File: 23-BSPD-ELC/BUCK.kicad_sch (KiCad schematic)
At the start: 0 parts

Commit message: Revision changes and updates to some footprints
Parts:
- added C32, C33: 10uF, Capacitor_SMD:C_0603_1608Metric_Pad1.08x0.95mm_HandSolder, symbol Device:C
- added C34, C35: 100nF, Capacitor_SMD:C_0603_1608Metric_Pad1.08x0.95mm_HandSolder, symbol Device:C
- added C36, C37: 22uF, Capacitor_SMD:C_0603_1608Metric_Pad1.08x0.95mm_HandSolder, symbol Device:C
- added L2: 4u7, Inductor_SMD:L_Sunlord_MWSA0518_5.4x5.2mm, symbol Device:L
- added R56, R57: 10K, Resistor_SMD:R_0603_1608Metric_Pad0.98x0.95mm_HandSolder, symbol Device:R
- added R58: 54.9K, Resistor_SMD:R_0603_1608Metric_Pad0.98x0.95mm_HandSolder, symbol Device:R
- added U19: LMR51420, Package_TO_SOT_SMD:SOT-23-6, symbol Regulator_Switching:TPS562200
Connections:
- new net 5V_out: C36.1, C37.1, L2.2, R58.2
- new net EN: R56.2, U19.5 (EN)
- new net GND: C32.2, C33.2, C34.2, C36.2, C37.2, R57.2, U19.1 (GND)
- new net SW: C35.1, L2.1, U19.2 (SW)
- new net VBST: C35.2, U19.6 (VBST)
- new net VFB: R57.1, R58.1, U19.4 (VFB)
- new net V_in: C32.1, C33.1, C34.1, R56.1, U19.3 (VIN)
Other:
- note added: "Pull EN high to enable (19V tolerant)"

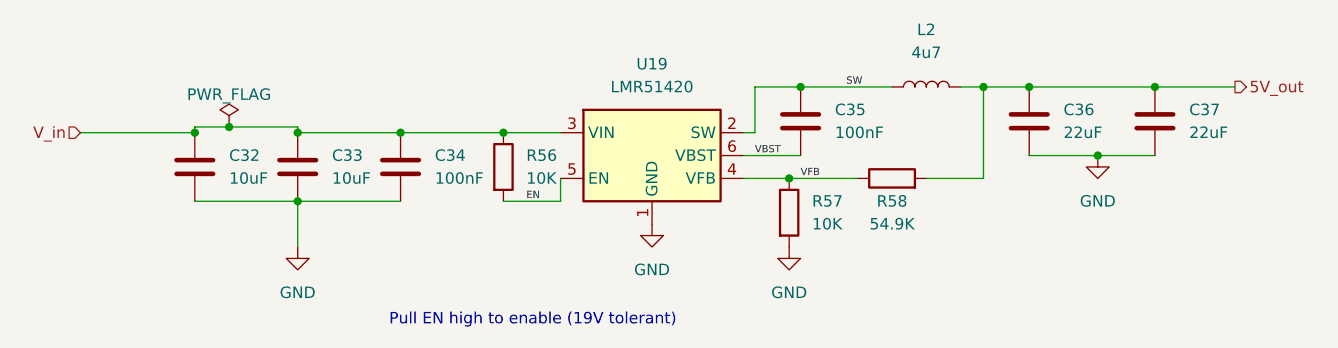
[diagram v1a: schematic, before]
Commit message: Updated pcb layout; Watchdog on board still in progress
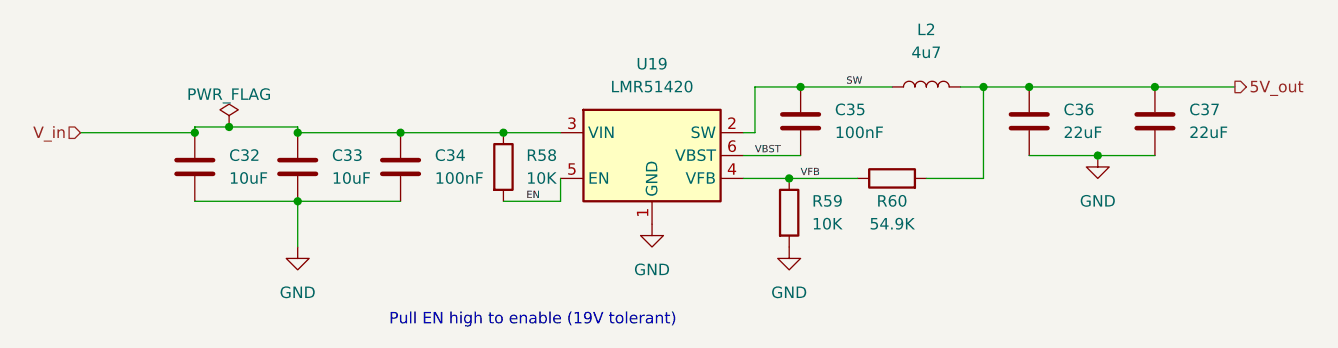
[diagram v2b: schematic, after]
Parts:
- renumbered R56 to R58, R57 to R59, R58 to R60
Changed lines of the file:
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@@
   (symbol (lib_id "Device:R") (at 170.18 84.455 90) (unit 1)
     (in_bom yes) (on_board yes)
-    (property "Reference" "R58" (id 0) (at 170.18 86.995 90))
+    (property "Reference" "R60" (id 0) (at 170.18 86.995 90))
     (property "Value" "54.9K" (id 1) (at 170.18 89.535 90))
     (property "Footprint" "Resistor_SMD:R_0603_1608Metric_Pad0.98x0.95mm_HandSolder" (id 2) (at 170.18 86.233 90)
@@
   (symbol (lib_id "Device:R") (at 127 83.185 0) (unit 1)
     (in_bom yes) (on_board yes) (fields_autoplaced)
-    (property "Reference" "R56" (id 0) (at 129.54 81.9149 0)
+    (property "Reference" "R58" (id 0) (at 129.54 81.9149 0)
       (effects (font (size 1.27 1.27)) (justify left))
     )
@@
   (symbol (lib_id "Device:R") (at 158.75 88.265 0) (unit 1)
     (in_bom yes) (on_board yes) (fields_autoplaced)
-    (property "Reference" "R57" (id 0) (at 161.29 86.9949 0)
+    (property "Reference" "R59" (id 0) (at 161.29 86.9949 0)
       (effects (font (size 1.27 1.27)) (justify left))
     )

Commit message: BSPD layout
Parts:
- renumbered C32 to C35, C33 to C36, C34 to C37, C35 to C38, C36 to C39, C37 to C40, R58 to R59, R59 to R60, R60 to R61, U19 to U20
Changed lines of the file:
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@@
   (symbol (lib_id "Device:C") (at 199.39 78.105 0) (unit 1)
     (in_bom yes) (on_board yes) (fields_autoplaced)
-    (property "Reference" "C37" (id 0) (at 203.2 76.8349 0)
+    (property "Reference" "C40" (id 0) (at 203.2 76.8349 0)
       (effects (font (size 1.27 1.27)) (justify left))
     )
@@
   (symbol (lib_id "power:GND") (at 193.04 81.915 0) (unit 1)
     (in_bom yes) (on_board yes) (fields_autoplaced)
-    (property "Reference" "#PWR0162" (id 0) (at 193.04 88.265 0)
+    (property "Reference" "#PWR0169" (id 0) (at 193.04 88.265 0)
       (effects (font (size 1.27 1.27)) hide)
     )
@@
   (symbol (lib_id "Device:C") (at 185.42 78.105 0) (unit 1)
     (in_bom yes) (on_board yes) (fields_autoplaced)
-    (property "Reference" "C36" (id 0) (at 189.23 76.8349 0)
+    (property "Reference" "C39" (id 0) (at 189.23 76.8349 0)
       (effects (font (size 1.27 1.27)) (justify left))
     )
@@
   (symbol (lib_id "Device:C") (at 92.71 83.185 0) (unit 1)
     (in_bom yes) (on_board yes) (fields_autoplaced)
-    (property "Reference" "C32" (id 0) (at 96.52 81.9149 0)
+    (property "Reference" "C35" (id 0) (at 96.52 81.9149 0)
       (effects (font (size 1.27 1.27)) (justify left))
     )
@@
   (symbol (lib_id "Device:C") (at 104.14 83.185 0) (unit 1)
     (in_bom yes) (on_board yes) (fields_autoplaced)
-    (property "Reference" "C33" (id 0) (at 107.95 81.9149 0)
+    (property "Reference" "C36" (id 0) (at 107.95 81.9149 0)
       (effects (font (size 1.27 1.27)) (justify left))
     )
@@
   (symbol (lib_id "Device:C") (at 115.57 83.185 0) (unit 1)
     (in_bom yes) (on_board yes) (fields_autoplaced)
-    (property "Reference" "C34" (id 0) (at 119.38 81.9149 0)
+    (property "Reference" "C37" (id 0) (at 119.38 81.9149 0)
       (effects (font (size 1.27 1.27)) (justify left))
     )
@@
   (symbol (lib_id "power:GND") (at 143.51 89.535 0) (unit 1)
     (in_bom yes) (on_board yes) (fields_autoplaced)
-    (property "Reference" "#PWR0160" (id 0) (at 143.51 95.885 0)
+    (property "Reference" "#PWR0167" (id 0) (at 143.51 95.885 0)
       (effects (font (size 1.27 1.27)) hide)
     )
@@
   (symbol (lib_id "Device:R") (at 170.18 84.455 90) (unit 1)
     (in_bom yes) (on_board yes)
-    (property "Reference" "R60" (id 0) (at 170.18 86.995 90))
+    (property "Reference" "R61" (id 0) (at 170.18 86.995 90))
     (property "Value" "54.9K" (id 1) (at 170.18 89.535 90))
     (property "Footprint" "Resistor_SMD:R_0603_1608Metric_Pad0.98x0.95mm_HandSolder" (id 2) (at 170.18 86.233 90)
@@
   (symbol (lib_id "Device:R") (at 127 83.185 0) (unit 1)
     (in_bom yes) (on_board yes) (fields_autoplaced)
-    (property "Reference" "R58" (id 0) (at 129.54 81.9149 0)
+    (property "Reference" "R59" (id 0) (at 129.54 81.9149 0)
       (effects (font (size 1.27 1.27)) (justify left))
     )
@@
   (symbol (lib_id "power:GND") (at 158.75 92.075 0) (unit 1)
     (in_bom yes) (on_board yes) (fields_autoplaced)
-    (property "Reference" "#PWR0161" (id 0) (at 158.75 98.425 0)
+    (property "Reference" "#PWR0168" (id 0) (at 158.75 98.425 0)
       (effects (font (size 1.27 1.27)) hide)
     )
@@
   (symbol (lib_id "Regulator_Switching:TPS562200") (at 143.51 81.915 0) (unit 1)
     (in_bom yes) (on_board yes) (fields_autoplaced)
-    (property "Reference" "U19" (id 0) (at 143.51 71.755 0))
+    (property "Reference" "U20" (id 0) (at 143.51 71.755 0))
     (property "Value" "LMR51420" (id 1) (at 143.51 74.295 0))
     (property "Footprint" "Package_TO_SOT_SMD:SOT-23-6" (id 2) (at 144.78 88.265 0)
@@
   (symbol (lib_id "Device:C") (at 160.02 78.105 0) (unit 1)
     (in_bom yes) (on_board yes) (fields_autoplaced)
-    (property "Reference" "C35" (id 0) (at 163.83 76.8349 0)
+    (property "Reference" "C38" (id 0) (at 163.83 76.8349 0)
       (effects (font (size 1.27 1.27)) (justify left))
     )
@@
   (symbol (lib_id "Device:R") (at 158.75 88.265 0) (unit 1)
     (in_bom yes) (on_board yes) (fields_autoplaced)
-    (property "Reference" "R59" (id 0) (at 161.29 86.9949 0)
+    (property "Reference" "R60" (id 0) (at 161.29 86.9949 0)
       (effects (font (size 1.27 1.27)) (justify left))
     )
@@
   (symbol (lib_id "power:GND") (at 104.14 92.075 0) (unit 1)
     (in_bom yes) (on_board yes) (fields_autoplaced)
-    (property "Reference" "#PWR0159" (id 0) (at 104.14 98.425 0)
-      (effects (font (size 1.27 1.27)) hide)
-    )
+    (property "Reference" "#PWR0166" (id 0) (at 104.14 98.425 0)
+      (effects (font (size 1.27 1.27)) hide)
+    )
